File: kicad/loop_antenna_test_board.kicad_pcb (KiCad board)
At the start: 2 copper layers, 57.2 x 27.9 mm, 4 parts

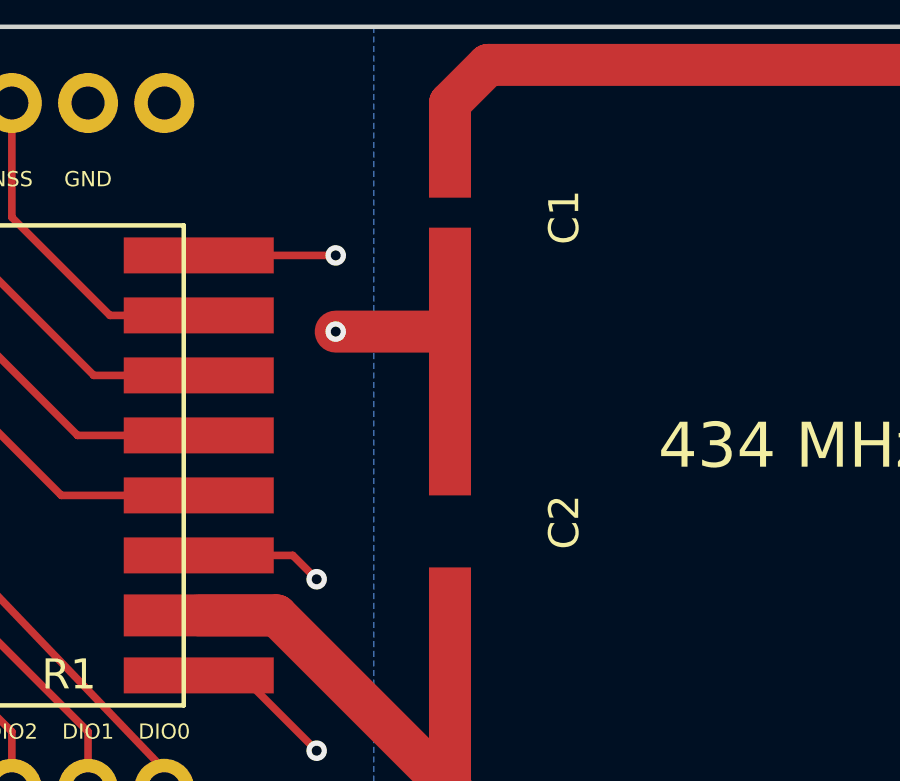
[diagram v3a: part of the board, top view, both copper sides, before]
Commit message: added outlines for capacitors
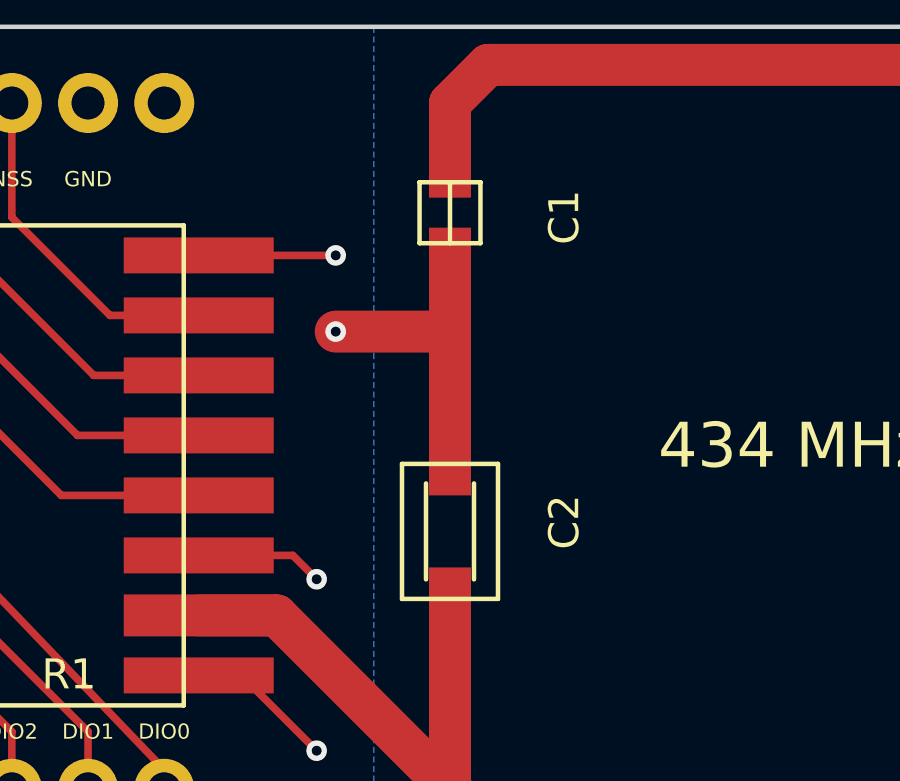
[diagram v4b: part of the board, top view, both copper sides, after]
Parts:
- C2: footprint loop_antenna_test_board:CAP_TUNABLE -> CAP_TUNABLE
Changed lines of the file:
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@@
     (links 19)
     (no_connects 0)
-    (area 126.924999 100.254999 186.765001 131.1024)
+    (area 126.924999 100.254999 184.225001 131.1024)
     (thickness 1.6)
     (drawings 24)
@@
     (add_net "Net-(R1-Pad15)")
   )
+  (module CAP_TUNABLE (layer F.Cu)
+    (at 160.02 114.3 270)
+    (fp_text reference C2 (at 2.54 -3.81 270) (layer F.SilkS)
+      (effects (font (size 1 1) (thickness 0.15)))
+    )
+    (fp_text value CTRIM (at 2.8 -2.4 270) (layer F.Fab)
+      (effects (font (size 1 1) (thickness 0.15)))
+    )
+    (fp_line (start 1.25 -0.8) (end 4.45 -0.8) (layer F.SilkS) (width 0.15))
+    (fp_line (start 1.25 0.8) (end 4.45 0.8) (layer F.SilkS) (width 0.15))
+    (fp_line (start 0.6 1.6) (end 0.6 -1.6) (layer F.SilkS) (width 0.15))
+    (fp_line (start 5.1 -1.6) (end 5.1 1.6) (layer F.SilkS) (width 0.15))
+    (fp_line (start 0.6 -1.6) (end 5.1 -1.6) (layer F.SilkS) (width 0.15))
+    (fp_line (start 0.6 1.6) (end 5.1 1.6) (layer F.SilkS) (width 0.15))
+    (pad 1 smd rect (at 0 0 270) (size 3.3 1.4) (layers F.Cu F.Mask)
+      (net 2 GND))
+    (pad 2 smd rect (at 5.7 0 270) (size 3.3 1.4) (layers F.Cu F.Mask)
+      (net 1 "Net-(C1-Pad1)"))
+  )
+  (module CAP (layer F.Cu)
+    (at 160.02 104.775 270)
+    (fp_text reference C1 (at 1.905 -3.81 270) (layer F.SilkS)
+      (effects (font (size 1 1) (thickness 0.15)))
+    )
+    (fp_text value C (at 2.0066 -1.8034 270) (layer F.Fab)
+      (effects (font (size 1 1) (thickness 0.15)))
+    )
+    (fp_line (start 0.7366 -1.016) (end 2.7686 -1.016) (layer F.SilkS) (width 0.15))
+    (fp_line (start 0.7366 1.016) (end 2.7686 1.016) (layer F.SilkS) (width 0.15))
+    (fp_line (start 2.7686 -1.016) (end 2.7686 1.016) (layer F.SilkS) (width 0.15))
+    (fp_line (start 0.7366 0) (end 2.7686 0) (layer F.SilkS) (width 0.15))
+    (fp_line (start 0.7366 -1.016) (end 0.7366 1.016) (layer F.SilkS) (width 0.15))
+    (pad 1 smd rect (at 0 0 270) (size 2.5 1.4) (layers F.Cu F.Mask)
+      (net 1 "Net-(C1-Pad1)"))
+    (pad 2 smd rect (at 3.5 0 270) (size 2.5 1.4) (layers F.Cu F.Mask)
+      (net 2 GND))
+  )
   (module RFM69W_BB (layer B.Cu)
     (at 142.875 115.57 180)
@@
       (net 2 GND))
   )
-  (module CAP (layer F.Cu)
-    (at 160.02 104.775 270)
-    (fp_text reference C1 (at 1.905 -3.81 270) (layer F.SilkS)
-      (effects (font (size 1 1) (thickness 0.15)))
-    )
-    (fp_text value C (at 2.0066 -1.8034 270) (layer F.Fab)
-      (effects (font (size 1 1) (thickness 0.15)))
-    )
-    (pad 1 smd rect (at 0 0 270) (size 2.5 1.4) (layers F.Cu F.Mask)
-      (net 1 "Net-(C1-Pad1)"))
-    (pad 2 smd rect (at 3.5 0 270) (size 2.5 1.4) (layers F.Cu F.Mask)
-      (net 2 GND))
-  )
-  (module loop_antenna_test_board:CAP_TUNABLE (layer F.Cu)
-    (at 160.02 114.3 270)
-    (fp_text reference C2 (at 2.54 -3.81 270) (layer F.SilkS)
-      (effects (font (size 1 1) (thickness 0.15)))
-    )
-    (fp_text value CTRIM (at 2.7178 -1.9558 270) (layer F.Fab)
-      (effects (font (size 1 1) (thickness 0.15)))
-    )
-    (pad 1 smd rect (at 0 0 270) (size 3.3 1.4) (layers F.Cu F.Mask)
-      (net 2 GND))
-    (pad 2 smd rect (at 5.7 0 270) (size 3.3 1.4) (layers F.Cu F.Mask)
-      (net 1 "Net-(C1-Pad1)"))
-  )
   (gr_line (start 184.15 125.73) (end 184.15 102.87) (angle 90) (layer Edge.Cuts) (width 0.15))
